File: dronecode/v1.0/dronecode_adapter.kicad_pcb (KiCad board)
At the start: 2 copper layers, 18 x 28 mm, 64 parts, among them J1 Jumper, J2 Jumper, J3 Jumper, J4 Jumper, X1 JTAG-10

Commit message: Updated jumper symbols in dronecode adapter.
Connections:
- PH1 pad 2: Net-(PH1-Pad2) -> (no net)
- PH4 pad 2: Net-(PH4-Pad2) -> (no net)
- PH4 pad 3: Net-(PH4-Pad3) -> (no net)
- X1 pad 6: /TDO -> (no net)
- X1 pad 7: Net-(X1-Pad7) -> (no net)

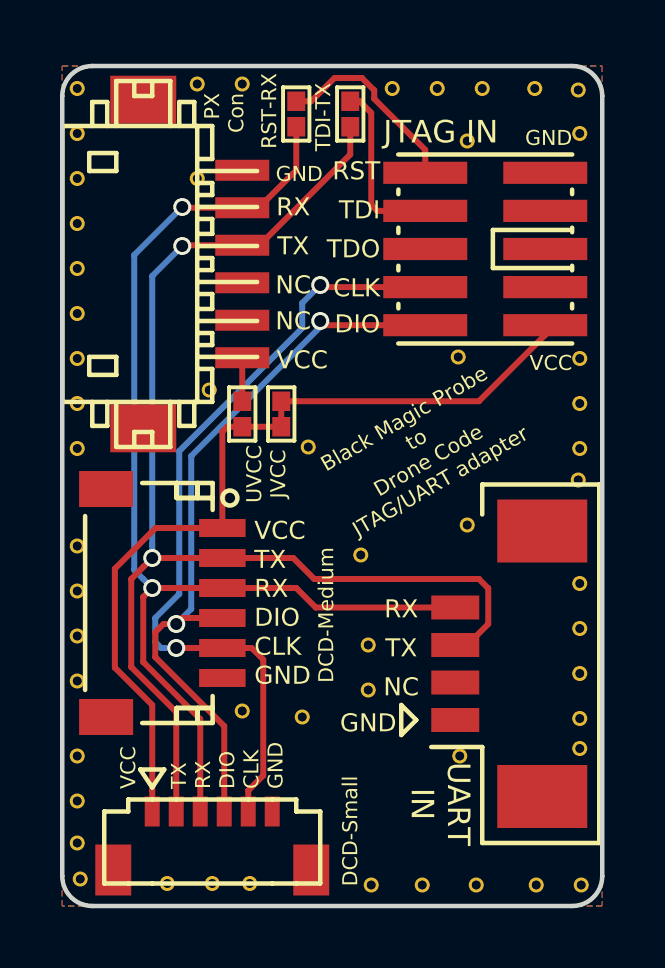
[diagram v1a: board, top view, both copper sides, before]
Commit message: Added pin 1 indicator on the 10pin connector.
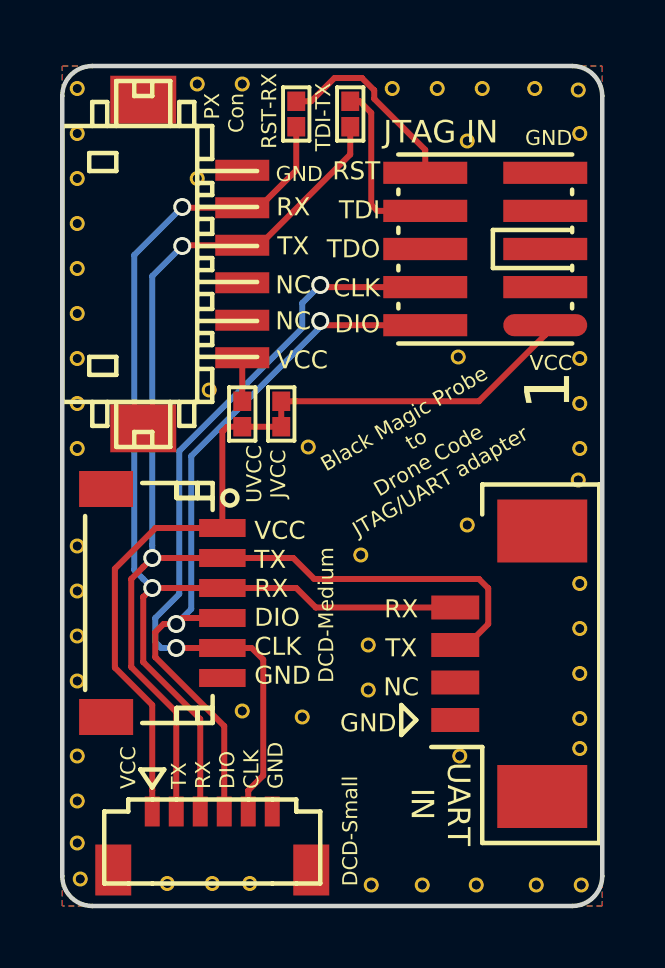
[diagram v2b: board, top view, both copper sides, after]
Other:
- board text added: "1"
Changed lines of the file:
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@@
-(kicad_pcb (version 4) (host pcbnew 4.0.6-e0-6349~53~ubuntu16.04.1)
+(kicad_pcb (version 4) (host pcbnew 4.0.7-e2-6376~58~ubuntu16.04.1)
   (general
     (links 80)
     (no_connects 0)
-    (area 19.924999 19.924999 38.075001 48.075001)
+    (area 16.7 15.3 47.85 50.425)
     (thickness 1.6)
-    (drawings 43)
+    (drawings 44)
     (tracks 108)
     (zones 0)
@@
     (mod_text_size 1 1)
     (mod_text_width 0.15)
-    (pad_size 0.65 0.6)
+    (pad_size 0.74 2.8)
     (pad_drill 0)
     (pad_to_mask_clearance 0.075)
@@
       (drillshape 0)
       (scaleselection 1)
-      (outputdirectory gerber))
+      (outputdirectory dronecode_gerber))
   )
   (net 0 "")
@@
     (fp_line (start -3.15 -2.9) (end -3.15 2.9) (layer F.SilkS) (width 0.15))
     (fp_line (start 3.15 -2.9) (end 3.15 2.9) (layer F.SilkS) (width 0.15))
-    (pad 1 smd rect (at -2.54 2 90) (size 0.74 2.8) (layers F.Cu F.Paste F.Mask)
+    (pad 1 smd oval (at -2.54 2 90) (size 0.74 2.8) (layers F.Cu F.Paste F.Mask)
       (net 8 VCC))
     (pad 2 smd rect (at -2.54 -2 90) (size 0.74 2.8) (layers F.Cu F.Paste F.Mask)
@@
     (fp_line (start -1 1) (end -1 5) (layer B.SilkS) (width 0.4))
   )
+  (gr_text 1 (at 36.2 30.8 90) (layer F.SilkS)
+    (effects (font (size 1.5 1.5) (thickness 0.3)))
+  )
   (dimension 18 (width 0.3) (layer Dwgs.User)
